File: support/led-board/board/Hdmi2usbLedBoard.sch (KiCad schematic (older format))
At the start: 33 parts, among them P1 CONN_20X2, Q1 OPTO_NPN

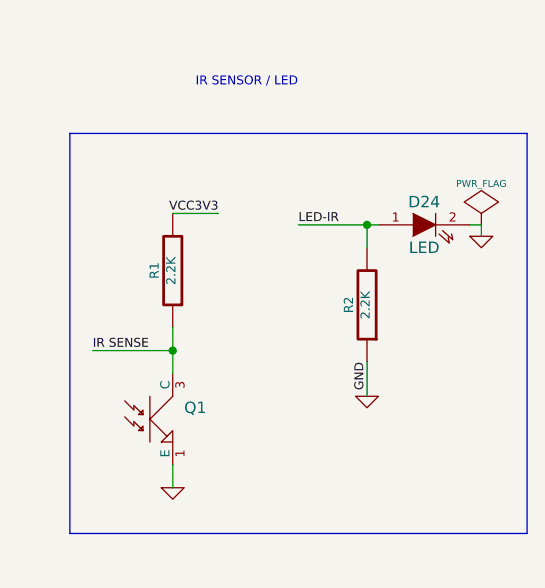
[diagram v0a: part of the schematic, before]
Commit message: Issue #1117 - LED board for HDMI
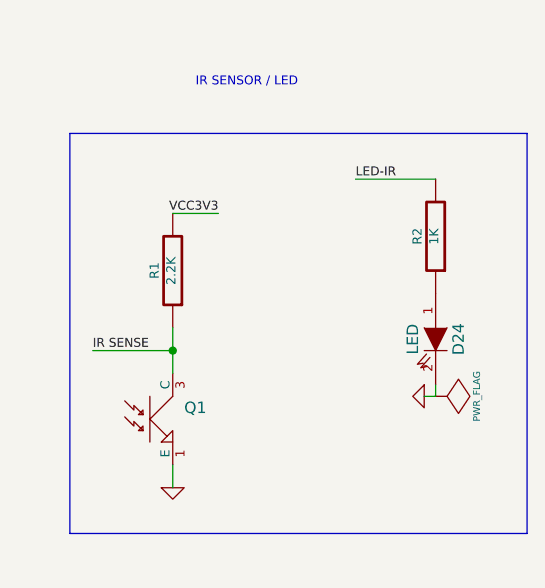
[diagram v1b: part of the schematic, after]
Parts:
- R2: value 2.2K -> 1K
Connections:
- net GND: no longer R2.1
- net LED-IR: no longer D24.1 (A)
- new net: D24.1 (A), R2.1
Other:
- moved on the sheet: D24, R2
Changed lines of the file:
@@
 LIBS:contrib
 LIBS:valves
-LIBS:Hdmi2usbLedDaughterBoard-cache
+LIBS:Hdmi2usbLedBoard-cache
 EELAYER 27 0
 EELAYER END
@@
 Sheet 1 1
 Title "HDMI2USB"
-Date "10 jun 2014"
+Date "19 jun 2014"
 Rev ""
 Comp ""
@@
 L LED D24
 U 1 1 53969A2D
-P 9900 4300
-F 0 "D24" H 9900 4400 50  0000 C CNN
-F 1 "LED" H 9900 4200 50  0000 C CNN
-F 2 "~" H 9900 4300 60  0000 C CNN
-F 3 "~" H 9900 4300 60  0000 C CNN
-	1    9900 4300
-	1    0    0    -1
+P 9950 4800
+F 0 "D24" H 9950 4900 50  0000 C CNN
+F 1 "LED" H 9950 4700 50  0000 C CNN
+F 2 "~" H 9950 4800 60  0000 C CNN
+F 3 "~" H 9950 4800 60  0000 C CNN
+	1    9950 4800
+	0    1    1    0
 $EndComp
 Wire Wire Line
 	4150 5950 4500 5950
 Wire Wire Line
-	9350 4300 9700 4300
-Wire Wire Line
-	10100 4300 10150 4300
+	9600 4100 9950 4100
+Wire Wire Line
+	9950 5000 9950 5050
 Wire Wire Line
 	4900 5950 4950 5950
 Text Label 4150 5950 0    39   ~ 0
 LED-PGOOD
-Text Label 9350 4300 0    39   ~ 0
+Text Label 9600 4100 0    39   ~ 0
 LED-IR
 Wire Wire Line
@@
 $EndComp
 Wire Wire Line
-	10150 4300 10150 4350
+	9950 5050 9900 5050
 $Comp
 L GND #PWR010
 U 1 1 53969E6A
-P 10150 4350
-F 0 "#PWR010" H 10150 4350 30  0001 C CNN
-F 1 "GND" H 10150 4280 30  0001 C CNN
-F 2 "" H 10150 4350 60  0000 C CNN
-F 3 "" H 10150 4350 60  0000 C CNN
-	1    10150 4350
-	1    0    0    -1
+P 9900 5050
+F 0 "#PWR010" H 9900 5050 30  0001 C CNN
+F 1 "GND" H 9900 4980 30  0001 C CNN
+F 2 "" H 9900 5050 60  0000 C CNN
+F 3 "" H 9900 5050 60  0000 C CNN
+	1    9900 5050
+	0    1    1    0
 $EndComp
 Text Notes 8900 3700 0    39   ~ 0
@@
 L PWR_FLAG #FLG011
 U 1 1 5396A01C
-P 10150 4300
-F 0 "#FLG011" H 10150 4395 30  0001 C CNN
-F 1 "PWR_FLAG" H 10150 4480 30  0000 C CNN
-F 2 "" H 10150 4300 60  0000 C CNN
-F 3 "" H 10150 4300 60  0000 C CNN
-	1    10150 4300
-	1    0    0    -1
+P 9950 5050
+F 0 "#FLG011" H 9950 5145 30  0001 C CNN
+F 1 "PWR_FLAG" H 9950 5230 30  0000 C CNN
+F 2 "" H 9950 5050 60  0000 C CNN
+F 3 "" H 9950 5050 60  0000 C CNN
+	1    9950 5050
+	0    1    1    0
 $EndComp
 Wire Bus Line
@@
 L R R2
 U 1 1 53969FCC
-P 9650 4650
-F 0 "R2" V 9730 4650 40  0000 C CNN
-F 1 "2.2K" V 9657 4651 40  0000 C CNN
-F 2 "~" V 9580 4650 30  0000 C CNN
-F 3 "~" H 9650 4650 30  0000 C CNN
-	1    9650 4650
+P 9950 4350
+F 0 "R2" V 10030 4350 40  0000 C CNN
+F 1 "1K" V 9957 4351 40  0000 C CNN
+F 2 "~" V 9880 4350 30  0000 C CNN
+F 3 "~" H 9950 4350 30  0000 C CNN
+	1    9950 4350
 	-1   0    0    1
 $EndComp
-Wire Wire Line
-	9650 4400 9650 4300
-Connection ~ 9650 4300
-Text Label 9650 4900 3    39   ~ 0
-GND
-Wire Wire Line
-	9650 4900 9650 5050
-$Comp
-L GND #PWR012
-U 1 1 5396A0AA
-P 9650 5050
-F 0 "#PWR012" H 9650 5050 30  0001 C CNN
-F 1 "GND" H 9650 4980 30  0001 C CNN
-F 2 "" H 9650 5050 60  0000 C CNN
-F 3 "" H 9650 5050 60  0000 C CNN
-	1    9650 5050
-	1    0    0    -1
-$EndComp
-Wire Bus Line
+Wire Bus Line
